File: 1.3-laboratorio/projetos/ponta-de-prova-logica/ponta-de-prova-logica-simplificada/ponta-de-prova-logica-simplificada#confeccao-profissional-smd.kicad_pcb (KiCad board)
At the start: 2 copper layers, 66 x 49.5 mm, 21 parts, among them J1 Conn_01x02, J2 PONTA DE PROVA, SW1 SW_DPDT_x2, U1 LM339

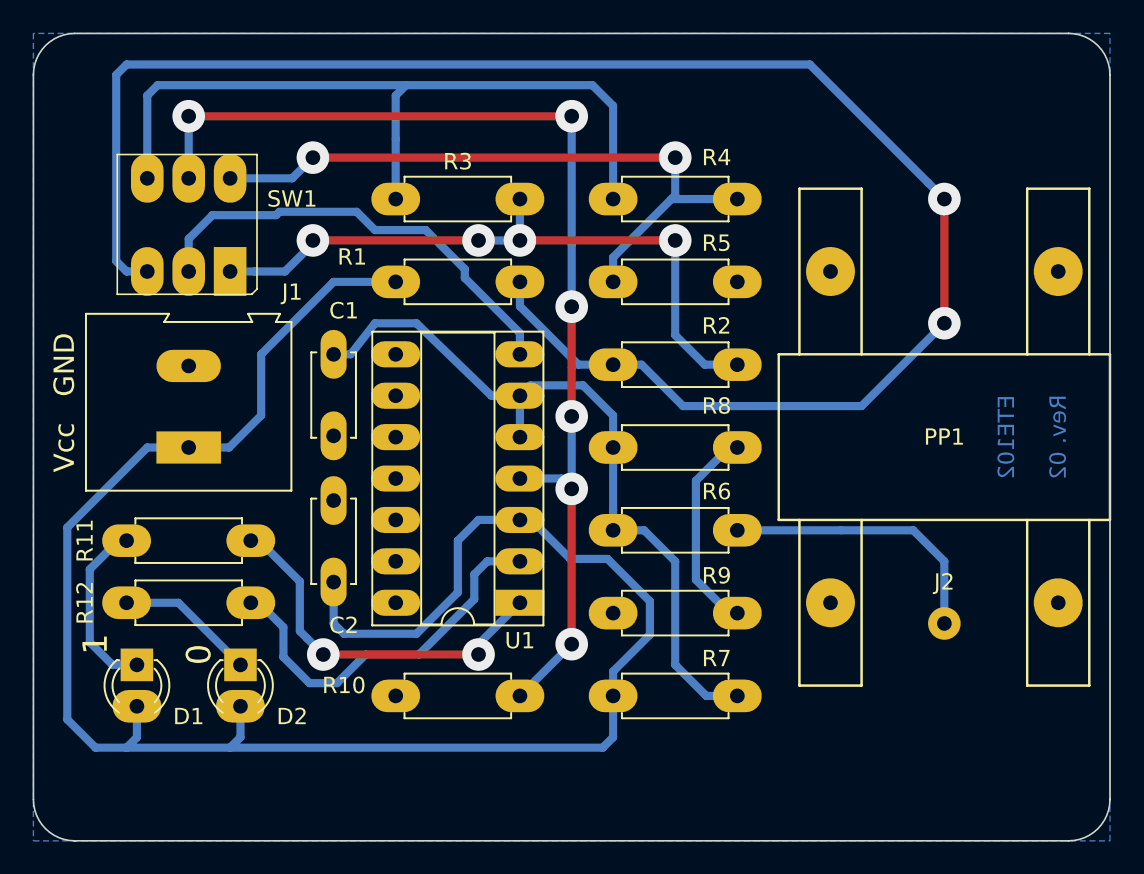
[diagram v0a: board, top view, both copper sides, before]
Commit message: Preparativos para o projeto da Ponta de Prova Lógica SMD.
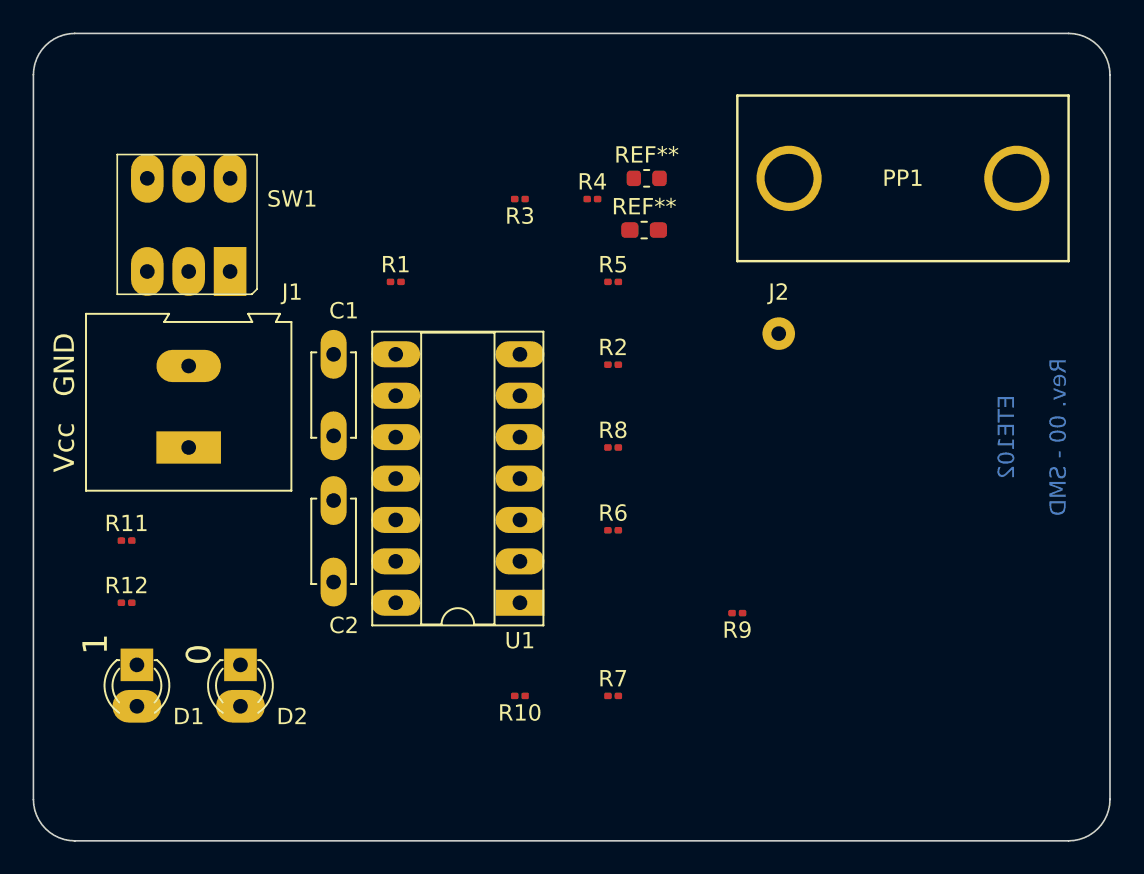
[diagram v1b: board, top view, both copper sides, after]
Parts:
- added REF**: R_0603_1608Metric, Resistor_SMD:R_0603_1608Metric, F.Cu at (55.4, 27.3)
- added REF**: R_0603_1608Metric_Pad1.05x0.95mm_HandSolder, Resistor_SMD:R_0603_1608Metric_Pad1.05x0.95mm_HandSolder, F.Cu at (55.2, 30.5)
- R1, R10, R11, R12, R2, R3, R4, R5, R6, R7, R8, R9: footprint Resistor_THT:R_Axial_DIN0207_L6.3mm_D2.5mm_P7.62mm_Horizontal -> Resistor_SMD:R_0201_0603Metric
- moved PP1 31.5 mm to (81.3, 22.2), turned to 270 degrees
- moved J2 20.5 mm to (63.5, 36.8)
- moved R4 1.27 mm to (52.1, 28.6)
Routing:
- net VCC: track 118.7 -> 0.00 mm
- net Net-(R1-Pad2): track 107.9 -> 0.00 mm, vias 2 -> 0
- net Net-(R10-Pad1): track 67.6 -> 0.00 mm, vias 6 -> 0
- net Net-(R3-Pad2): track 47.4 -> 0.00 mm
- net Net-(C1-Pad1): track 46.0 -> 0.00 mm
- net Net-(R2-Pad2): track 41.1 -> 0.00 mm, vias 4 -> 0
- net Net-(R4-Pad2): track 41.1 -> 0.00 mm, vias 2 -> 0
- net Net-(SW1-Pad2): track 27.7 -> 0.00 mm
- net Net-(R12-Pad2): track 23.6 -> 0.00 mm
- net Net-(R11-Pad2): track 22.9 -> 0.00 mm, vias 2 -> 0
- net Net-(J2-Pad1): track 17.3 -> 0.00 mm
- net Net-(R8-Pad2): track 12.8 -> 0.00 mm
- net Net-(D1-Pad1): track 10.9 -> 0.00 mm
- net Net-(D2-Pad1): track 8.56 -> 0.00 mm
- removed copper zone on B.Cu, net GND
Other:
- board text added: "Rev. 00 - SMD"
- board text removed: "Rev. 02"
